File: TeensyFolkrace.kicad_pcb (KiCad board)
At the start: 2 copper layers, 49.3 x 48.8 mm, 30 parts, among them P1 MOTOR, P2 STEERING, P3 START, P4 BATT, U1 Teensy31_32, U10 ADXL345_Breakout, U2 WS2812B, U3 WS2812B, U4 TCA9548APWR, U5 SEN1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

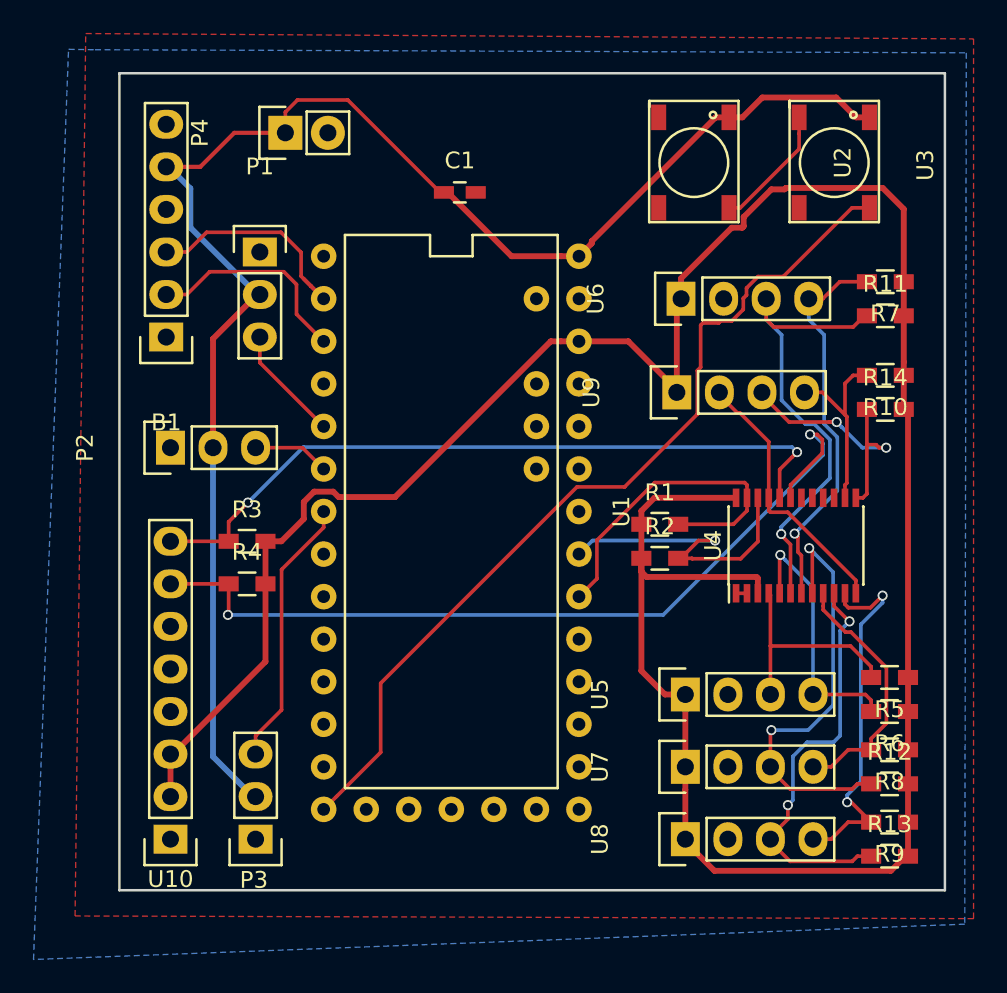
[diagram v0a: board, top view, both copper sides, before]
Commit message: Added reset-resistor, and generated gerbers
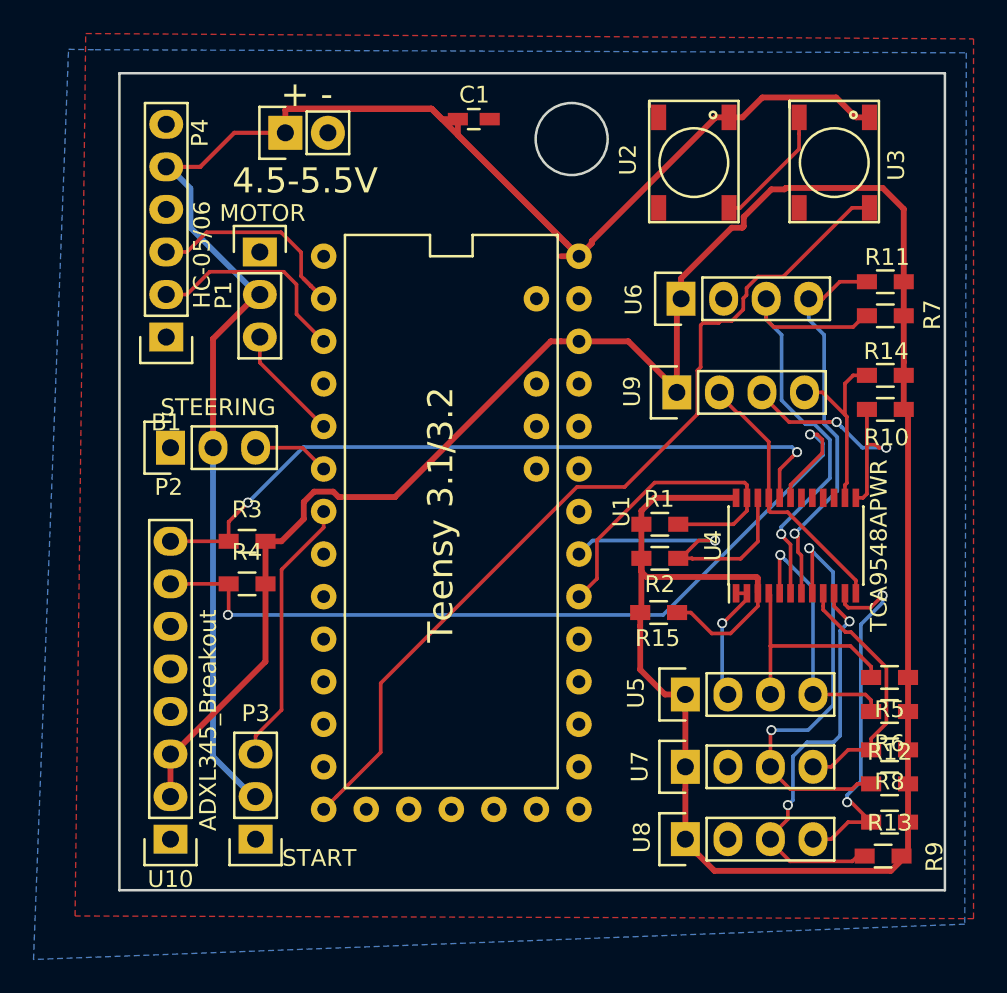
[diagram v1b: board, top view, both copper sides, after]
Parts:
- added R15: R, Resistors_SMD:R_0603_HandSoldering, F.Cu at (132.3, 83.5)
- moved C1 4.45 mm to (121.2, 54.0)
- moved R13 0.39 mm to (145.7, 98.0)
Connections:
- B1 pad 1: Net-(B1-Pad1) -> (no net)
- B1 pad 6: Net-(B1-Pad6) -> (no net)
- U1 pad 10: Net-(U1-Pad10) -> (no net)
- U1 pad 11: Net-(U1-Pad11) -> (no net)
- U1 pad 13: Net-(U1-Pad13) -> (no net)
- U1 pad 14: Net-(U1-Pad14) -> (no net)
- U1 pad 15: Net-(U1-Pad15) -> (no net)
- U1 pad 16: Net-(U1-Pad16) -> (no net)
- U1 pad 17: Net-(U1-Pad17) -> (no net)
- U1 pad 2: Net-(U1-Pad2) -> (no net)
- U1 pad 20: Net-(U1-Pad20) -> (no net)
- U1 pad 21: Net-(U1-Pad21) -> (no net)
- U1 pad 22: Net-(U1-Pad22) -> (no net)
- U1 pad 23: Net-(U1-Pad23) -> (no net)
- U1 pad 28: Net-(U1-Pad28) -> (no net)
- U1 pad 29: Net-(U1-Pad29) -> (no net)
- U1 pad 30: Net-(U1-Pad30) -> (no net)
- U1 pad 31: Net-(U1-Pad31) -> (no net)
- U1 pad 32: Net-(U1-Pad32) -> (no net)
- U1 pad 33: Net-(U1-Pad33) -> (no net)
- U1 pad 35: Net-(U1-Pad35) -> (no net)
- U1 pad 36: Net-(U1-Pad36) -> (no net)
- U1 pad 6: Net-(U1-Pad6) -> (no net)
- U1 pad 7: Net-(U1-Pad7) -> (no net)
- U1 pad 8: Net-(U1-Pad8) -> (no net)
- U1 pad 9: Net-(U1-Pad9) -> (no net)
- U10 pad 4: Net-(U10-Pad4) -> (no net)
- U10 pad 5: Net-(U10-Pad5) -> (no net)
- U10 pad 6: Net-(U10-Pad6) -> (no net)
- U2 pad 2: Net-(U2-Pad2) -> (no net)
- U4 pad 15: Net-(U4-Pad15) -> (no net)
- U4 pad 16: Net-(U4-Pad16) -> (no net)
- U4 pad 17: Net-(U4-Pad17) -> (no net)
- U4 pad 18: Net-(U4-Pad18) -> (no net)
- U4 pad 3: +3V3 -> Net-(R15-Pad2)
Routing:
- net +5V: track 95.2 -> 118.8 mm
- net Net-(R15-Pad2): track 0.00 -> 7.69 mm
- net GND: track 17.1 -> 23.9 mm, vias 0 -> 1
- net +3V3: track 162.3 -> 161.4 mm
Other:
- outline, holes or cut-outs redrawn
- board text added: "+ -"
- board text added: "4.5-5.5V"
- board text added: "Frode Lillerud 19.jan 2016"
- board text added: "Teensy 3.1/3.2"
- board text removed: "Frode Lillerud 4.jan 2016"
